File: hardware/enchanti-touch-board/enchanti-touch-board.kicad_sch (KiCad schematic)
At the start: 92 parts, among them J2 Progamming Header, U1 CY8C4149AZI-S598

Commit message: Updated manufacturing files for board-rev3, added CANFD connector from board, removed redundant I2C connector
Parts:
- removed GPIO1, GPIO2: I2C, JST-footprints:JST_SH_BM04B-SRSS-TB_1x04-1MP_P1.00mm_Vertical, symbol Connector_Generic_MountingPin:Conn_01x04_MountingPin
- removed GPIO3: SPI1, JST-footprints:JST_SH_BM04B-SRSS-TB_1x04-1MP_P1.00mm_Vertical, symbol Connector_Generic_MountingPin:Conn_01x04_MountingPin
- removed GPIO4: SPI2, JST-footprints:JST_SH_BM04B-SRSS-TB_1x04-1MP_P1.00mm_Vertical, symbol Connector_Generic_MountingPin:Conn_01x04_MountingPin
- removed J2: Progamming Header, Connector_PinHeader_1.27mm:PinHeader_2x05_P1.27mm_Vertical_SMD, symbol Connector_Generic:Conn_02x05_Odd_Even
- added C59: 1uF, Capacitor_SMD:C_0402_1005Metric, symbol Device:C
- added C61, C66: 0.1uF, Capacitor_SMD:C_0402_1005Metric, symbol Device:C
- added CANFD1, CANFD2, I2C1: JST-SH-1x04 1.0mm, ENCHANTI_connectors:JST_SMD_1.0mm-4_Vertical, symbol ENCHANTI_connectors:QWIIC-CONNECTOR
- added D2, D3: NUP2105L, Package_TO_SOT_SMD:SOT-23, symbol Power_Protection:NUP2105L
- added J1: Programming Header, ENCHANTI_connectors:SAMTEC_FTSH-105-01-F-DV-P-TR, symbol ENCHANTI_connectors:Programming_Header
- added R65: 120, Resistor_SMD:R_0805_2012Metric_Pad1.20x1.40mm_HandSolder, symbol Device:R_US
- added R66, R67: 330, Resistor_SMD:R_0201_0603Metric, symbol Device:R_US
- added R71, R72: 10k, Resistor_SMD:R_0402_1005Metric, symbol Device:R_US
- added SW2: SW_DIP_x02, ENCHANTI_switches:TDA02H0SB1R_CNK, symbol Switch:SW_DIP_x02
- added U8: TCAN3413DRBR, ENCHANTI_transceivers:VSON8-DRB_TEX, symbol ENCHANTI_transceivers:TCAN3413DRBR
- C1, C10, C12, C14, C3, C5: Mfg Part # (none) -> GCM155R71C104KA55J
- C11, C13, C15, C18, C2, C4: Description Value Pkg (none) -> 1 µF ±10% 16V Ceramic Capacitor X5R 0402 (1005 Metric); Mfg Part # (none) -> GRM155R61C105KA12D
- C6, C7, C8, C9: Mfg Part # (none) -> GRM155R71H222JA01J
- D1: Mfg Part # (none) -> ESD5V0D5-TP
- GPIO5: now left out of the parts list
- R1, R2: Mfg Part # (none) -> ERJ-1GNF3300C
- R10, R11, R12, R13, R14, R15, R16, R17, R18, R19, R20, R21, R22, R23, R24, R25, R26, R27, R28, R29, R3, R30, R31, R32, R33, R34, R35, R36, R37, R38, R39, R4, R40, R41, R42, R43, R44, R45, R46, R47, R48, R49, R5, R50, R51, R52, R53, R54, R55, R56, R57, R58, R59, R6, R60, R61, R62, R7, R8, R9: Mfg Part # (none) -> ERJ-1GNF5600C
- R63, R64: Mfg Part # (none) -> ERJ-1GNF4701C
- TOUCH1, TOUCH2: Mfg Part # (none) -> 54132-3262
- U1: Mfg Part # (none) -> CY8C4149AZI-S598
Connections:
- net +3V3: now also C59.1, C61.1, C66.1, CANFD1.2 (3v3), CANFD2.2 (3v3), I2C1.2 (3v3), J1.1 (VDD), SW2.3, SW2.4, U8.3 (VCC), U8.5 (VIO)
- net EVT_MAIN: now also GPIO5.1 (Pin_1); no longer GPIO5.2 (Pin_2)
- net GND: now also C59.2, C61.2, C66.2, CANFD1.1 (GND), CANFD2.1 (GND), D2.3 (A), D3.3 (A), I2C1.1 (GND), J1.3 (GND), J1.5 (GND), J1.9 (GND), R71.1, R72.1, U8.2 (GND), U8.9 (EPAD)
- net MSC022: now also R23.1; no longer R25.1
- net MSC023: now also R24.1; no longer R26.1
- net MSC024: now also R25.1; no longer R27.1
- net MSC025: now also R26.1; no longer R28.1
- net MSC026: now also R27.1; no longer R29.1
- net MSC027: now also R28.1; no longer R30.1
- net MSC028: now also R29.1; no longer R31.1
- net MSC029: now also R30.1; no longer R32.1
- net POLL_MAIN: now also GPIO5.2 (Pin_2); no longer GPIO5.1 (Pin_1)
- net RES: now also J1.10 (RES)
- net SCL: now also I2C1.4 (SCL)
- net SDA: now also I2C1.3 (SDA)
- net SWCLK: now also J1.4 (SWCLK)
- net SWDA: now also J1.2 (SWDIO)
- net MSC030: now reaches U1.27 (P3.0)
- net MSC030: now also R31.1
- net MSC031: now reaches U1.28 (P3.1)
- net MSC031: now also R32.1
- net CIPO_AUX: no longer names the net of U1.37 (P11.1)
- net CIPO_MAIN: no longer names the net of U1.48 (P4.5)
- net COPI_AUX: no longer names the net of U1.36 (P11.0)
- net COPI_MAIN: no longer names the net of U1.47 (P4.4)
- net CS_AUX: no longer names the net of U1.39 (P11.3)
- net CS_MAIN renamed POS_P2
- net POS_P2: now also R67.1, R71.2
- net MSC020 renamed FDCAN1_RX
- net FDCAN1_RX: now also U8.4 (RXD); no longer R23.1
- net MSC021 renamed FDCAN1_TX
- net FDCAN1_TX: now also U8.1 (TXD); no longer R24.1
- net SCLK_AUX: no longer names the net of U1.38 (P11.2)
- net SCLK_MAIN renamed POS_P1
- net POS_P1: now also R66.1, R72.2
- net SPIMODE renamed CAN_MODE
- net CAN_MODE: now also U8.8 (STB)
- new net: CANFD2.NC1 (NC), CANFD2.NC2 (NC)
- new net: I2C1.NC1 (NC), I2C1.NC2 (NC)
- new net: CANFD1.NC1 (NC), CANFD1.NC2 (NC)
- new net CAN_H: CANFD1.3 (SDA), CANFD2.3 (SDA), D2.2 (K), D3.2 (K), R65.2, U8.7 (CANH)
- new net CAN_L: CANFD1.4 (SCL), CANFD2.4 (SCL), D2.1 (K), D3.1 (K), R65.1, U8.6 (CANL)
- new net P1: R66.2, SW2.1
- new net P2: R67.2, SW2.2
- no-connect marks 7 -> 3
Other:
- note added: "ADDRESS SELECTION"
- note added: "Bypass Capacitors"
- note added: "CAN TRANSCEIVER"
- note added: "CANFD Connectors"
- note added: "ESD Protection"
- note added: "Pulldown on all the address pins"
- note added: "Resistors to limit current into I2C pins"
- note added: "Touch board Position Selection Pos P1 P2 Pos 0: 0 0 Pos 1: 0 1 Pos 2: 1 0 Pos 3: 1 1"
- note removed: "4 Pin header for SPI"
- note removed: "Connect to Extra Touch board"
- note removed: "Connect to MCU"
- note removed: "I2C"
- moved on the sheet: C18, C3, C6, C7, C8, C9, D1, R1, R2

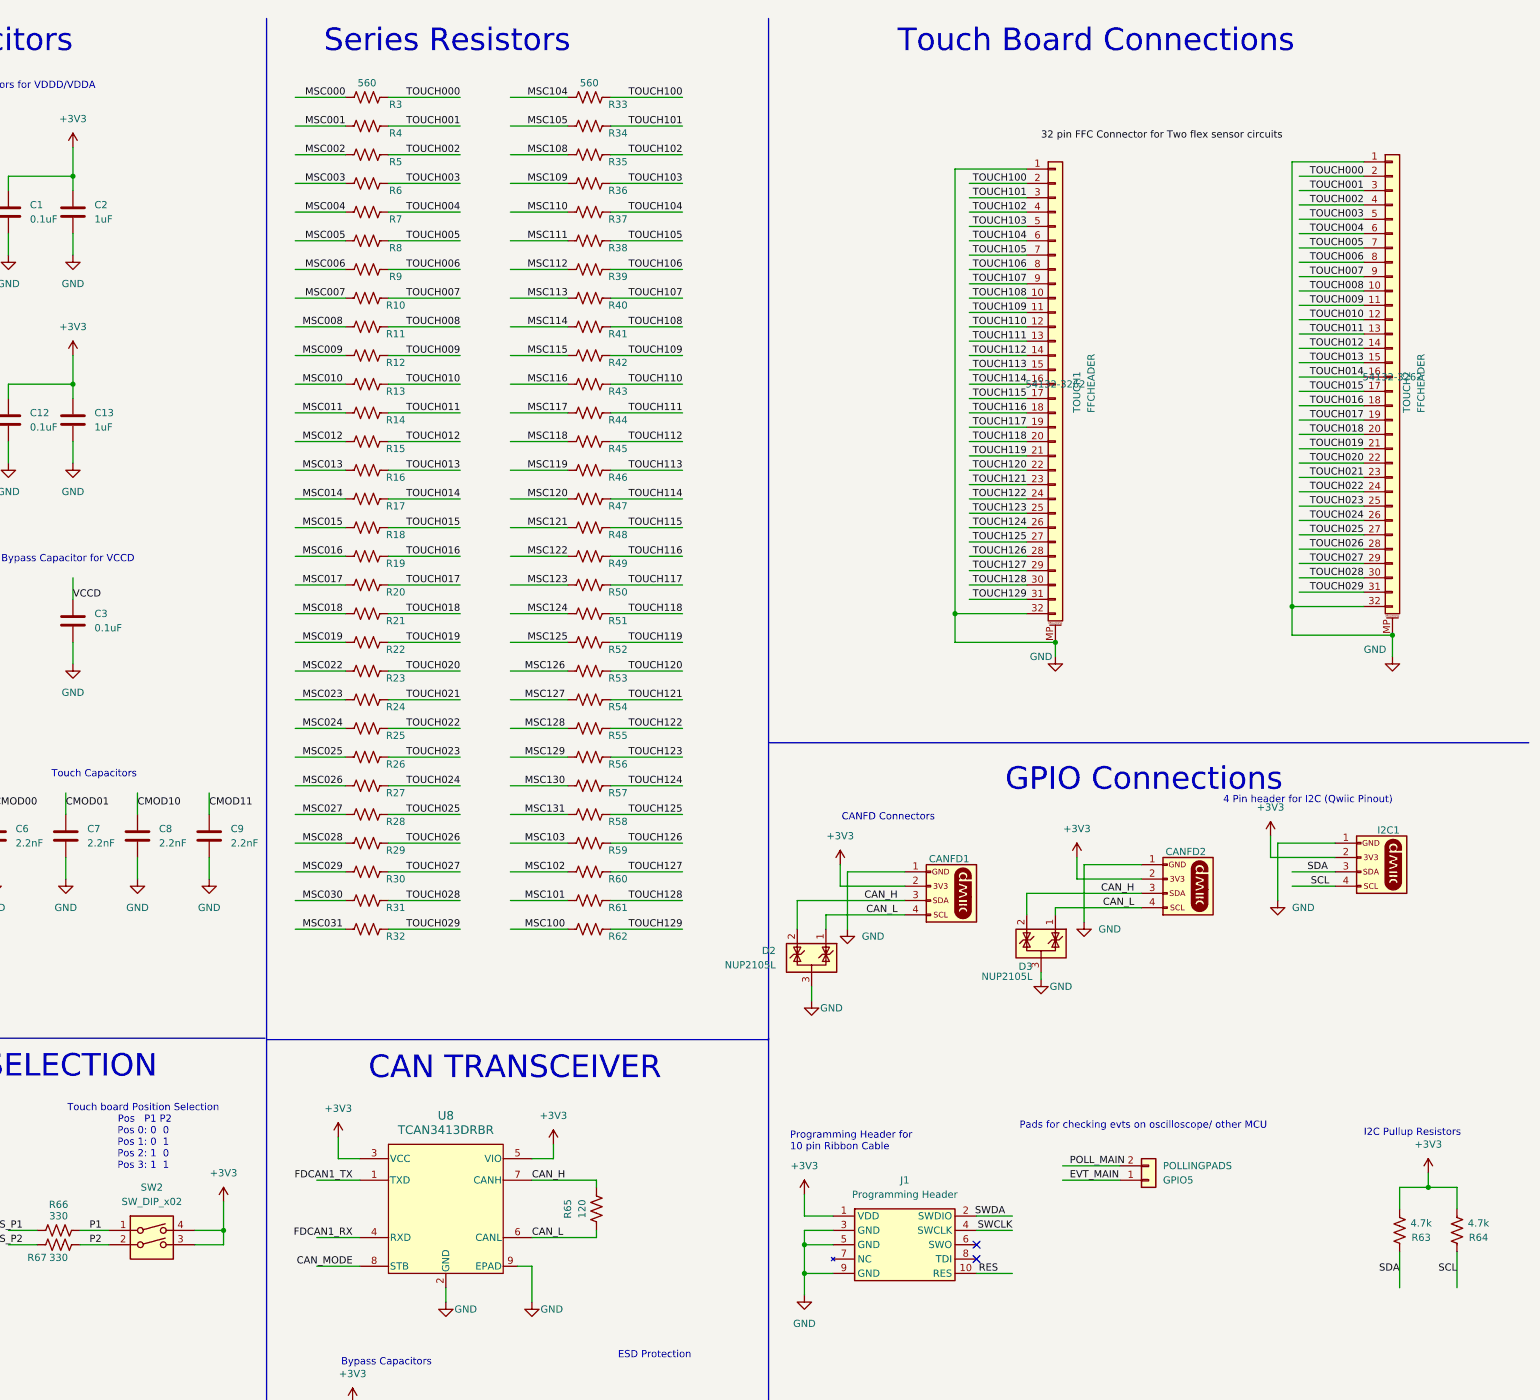
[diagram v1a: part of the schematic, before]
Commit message: Added comments to schematics for improvements in Rev 0.4
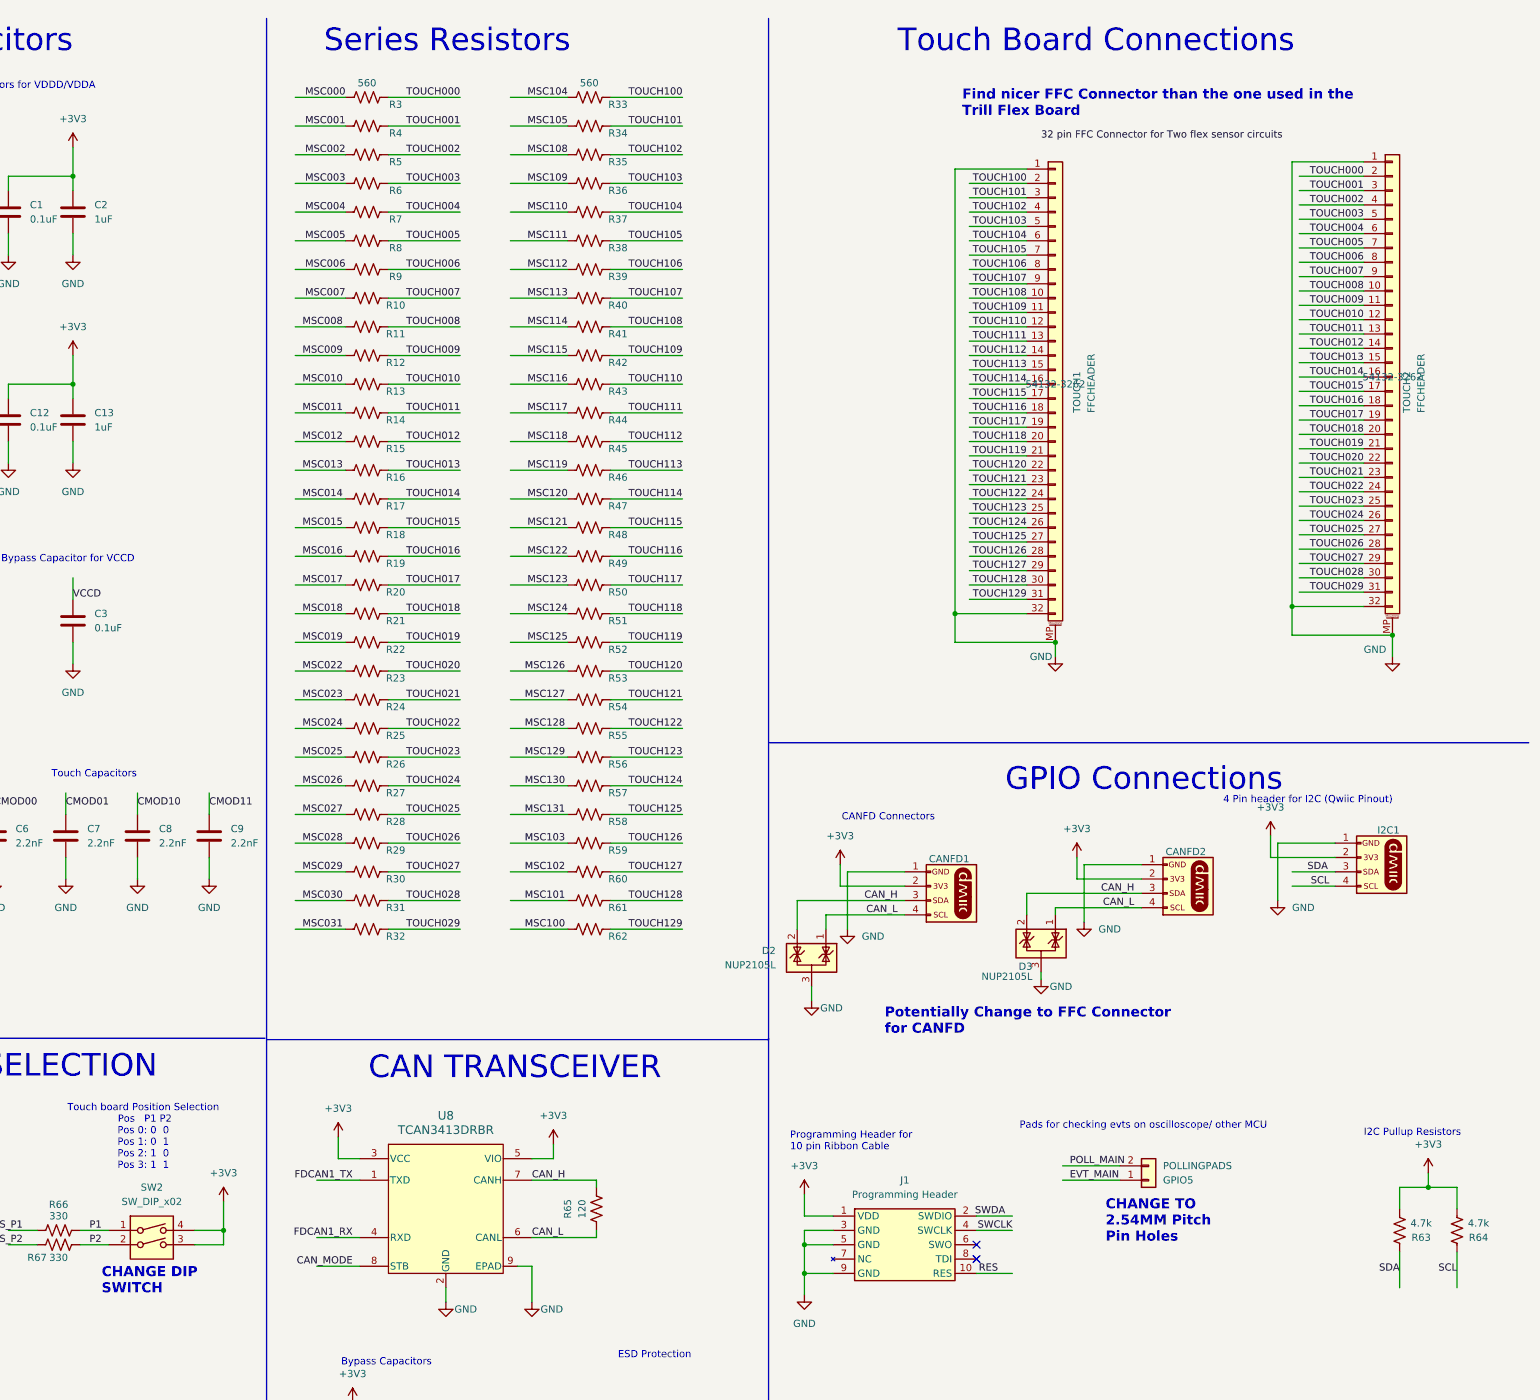
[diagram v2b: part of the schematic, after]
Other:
- note added: "CHANGE DIP SWITCH"
- note added: "CHANGE TO 2.54MM Pitch Pin Holes"
- note added: "Find nicer FFC Connector than the one used in the Trill Flex Board"
- note added: "Potentially Change to FFC Connector for CANFD"
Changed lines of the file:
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@@
+		)
+	)
+	(text "Potentially Change to FFC Connector\nfor CANFD"
+		(exclude_from_sim no)
+		(at 293.624 192.786 0)
+		(effects
+			(font
+				(size 1.778 1.778)
+				(thickness 0.3556)
+				(bold yes)
+				(color 255 0 0 1)
+			)
+			(justify left bottom)
+		)
+	)
+	(text "CHANGE TO\n2.54MM Pitch\nPin Holes"
+		(exclude_from_sim no)
+		(at 332.74 229.616 0)
+		(effects
+			(font
+				(size 1.778 1.778)
+				(thickness 0.3556)
+				(bold yes)
+				(color 255 0 0 1)
+			)
+			(justify left bottom)
 		)
 	)
@@
 		)
 	)
+	(text "Find nicer FFC Connector than the one used in the \nTrill Flex Board"
+		(exclude_from_sim no)
+		(at 307.34 30.226 0)
+		(effects
+			(font
+				(size 1.778 1.778)
+				(thickness 0.3556)
+				(bold yes)
+				(color 255 0 0 1)
+			)
+			(justify left bottom)
+		)
+	)
 	(text "CAN TRANSCEIVER"
 		(exclude_from_sim no)
@@
 			)
 			(justify left bottom)
+		)
+	)
+	(text "CHANGE DIP \nSWITCH"
+		(exclude_from_sim no)
+		(at 154.94 238.76 0)
+		(effects
+			(font
+				(size 1.778 1.778)
+				(thickness 0.3556)
+				(bold yes)
+				(color 255 0 0 1)
+			)
+			(justify left bottom)
